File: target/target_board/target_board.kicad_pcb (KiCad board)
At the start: 2 copper layers, 76 x 68 mm, 72 parts, among them J1 USB_B_Micro, J2 SPI_CONN, J3 UART_CONN, J4 I2C_CONN, J5 SWD_CONN, J6 DFU, Q1 RZM001P02, Q2 RZM001P02, SW1 SW_Push, SW10 SW_Push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

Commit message: Continue layout
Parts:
- moved D3 7.20 mm to (34.7, 71.2)
- moved R8 6.62 mm to (34.6, 69.4), turned to 0 degrees
- moved D2 5.10 mm to (34.7, 67.6)
- moved R6 5.04 mm to (34.6, 65.8), turned to 0 degrees
- moved R5 4.00 mm to (34.6, 62.2), turned to 0 degrees
- moved D1 3.00 mm to (34.7, 64.0)
- moved R20 0.40 mm to (57.2, 73.5)
- moved R21 0.40 mm to (57.2, 72.0)
- moved R22 0.40 mm to (57.2, 70.5)
- moved R23 0.40 mm to (57.2, 69.0)
- moved R24 0.40 mm to (57.2, 67.5)
- moved R25 0.40 mm to (57.2, 66.0)
- moved R26 0.40 mm to (57.2, 64.5)
- moved R27 0.40 mm to (57.2, 63.0)
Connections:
- U3 pad 10: /LED_G -> /COL2
- U3 pad 11: /LED_Y -> /COL1
- U3 pad 12: /LED_R -> /ROW4
- U3 pad 13: Net-(U3-Pad13) -> /DISPA
- U3 pad 22: Net-(U3-Pad22) -> /DISPB
- U3 pad 39: /ROW4 -> /LED_R
- U3 pad 40: /DISPA -> Net-(U3-Pad40)
- U3 pad 41: /DISPB -> Net-(U3-Pad41)
- U3 pad 45: /COL1 -> /LED_Y
- U3 pad 46: /COL2 -> /LED_G
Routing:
- net VCC: track 0.00 -> 200.7 mm
- net /SCL: track 0.00 -> 111.2 mm, vias 0 -> 5
- net /SDA: track 0.00 -> 104.2 mm, vias 0 -> 5
- net /UART1_RX: track 0.00 -> 97.4 mm, vias 0 -> 2
- net /UART1_TX: track 0.00 -> 94.8 mm, vias 0 -> 2
- net GND: track 0.00 -> 50.3 mm, vias 0 -> 16
- net /ROW4: track 0.00 -> 36.0 mm
- net /ROW3: track 0.00 -> 36.0 mm
- net /ROW2: track 0.00 -> 36.0 mm
- net /ROW1: track 0.00 -> 36.0 mm
- net /COL3: track 0.00 -> 31.8 mm
- net /COL2: track 0.00 -> 31.8 mm
- net /COL1: track 0.00 -> 31.8 mm
- net /LED_G: track 0.00 -> 20.6 mm
- net /NRST: track 0.00 -> 19.5 mm
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- added copper zone on B.Cu, net GND

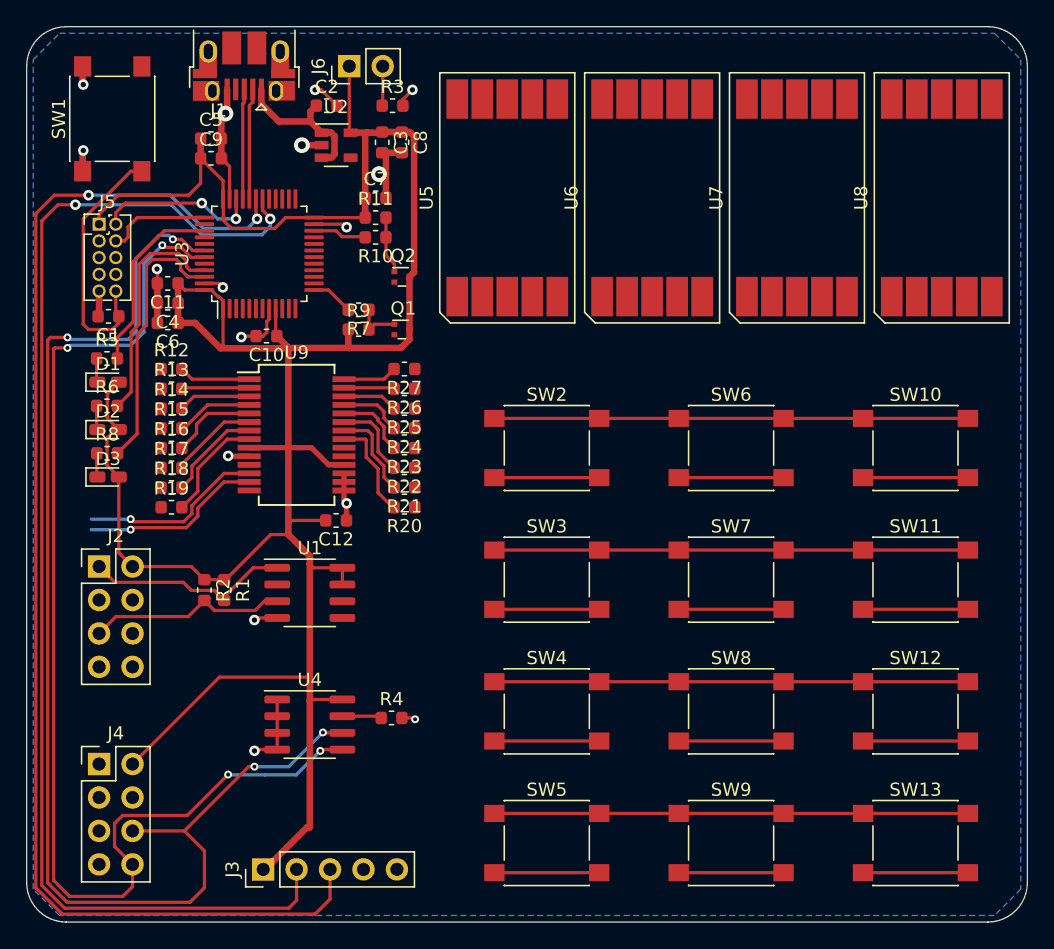
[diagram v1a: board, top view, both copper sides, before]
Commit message: Route busses.
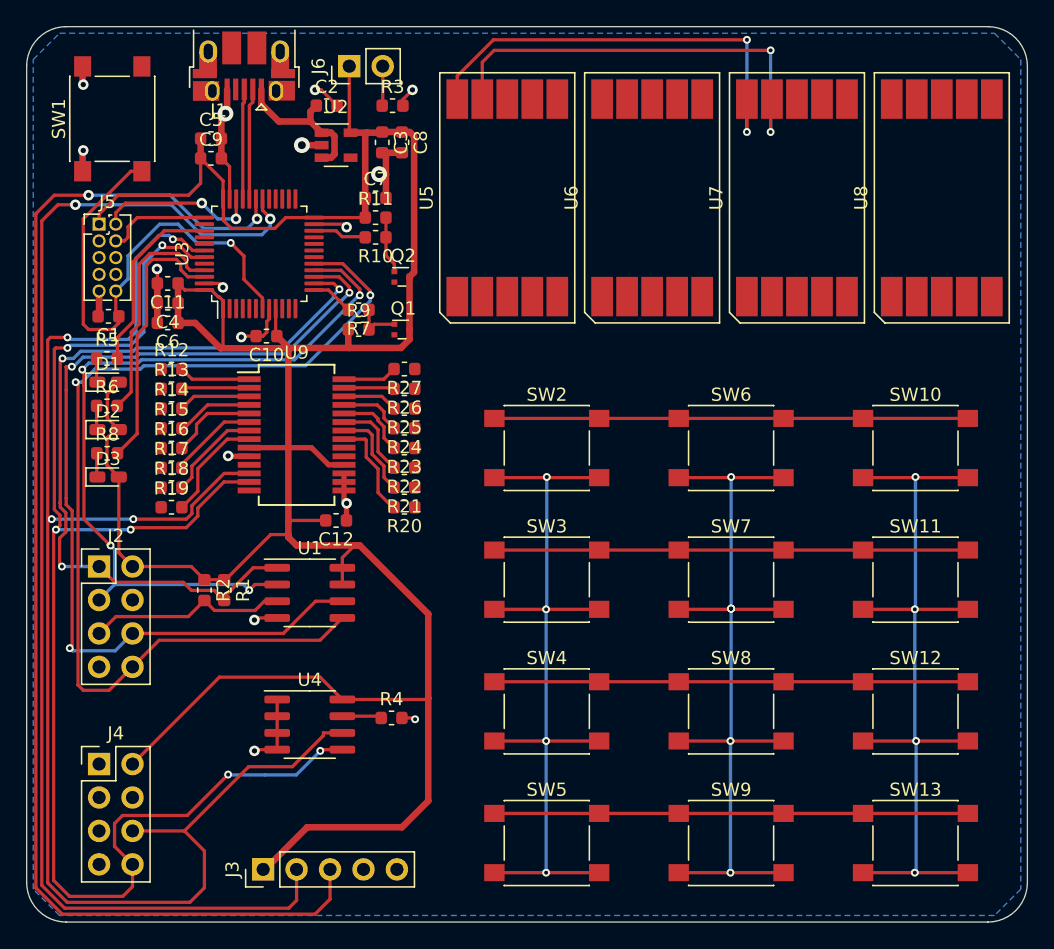
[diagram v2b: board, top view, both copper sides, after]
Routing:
- net /MOSI: track 0.00 -> 76.4 mm, vias 0 -> 2
- net /SCK: track 0.00 -> 71.2 mm, vias 0 -> 3
- net /MISO: track 0.00 -> 59.8 mm, vias 0 -> 4
- net /~CS: track 15.8 -> 60.4 mm, vias 0 -> 3
- net /A7: track 0.00 -> 34.4 mm, vias 0 -> 2
- net /A6: track 0.00 -> 33.8 mm, vias 0 -> 2
- net /COL3: track 31.8 -> 62.1 mm, vias 0 -> 4
- net /COL2: track 31.8 -> 62.0 mm, vias 0 -> 5
- net /COL1: track 31.8 -> 62.0 mm, vias 0 -> 4
- net VCC: track 200.7 -> 221.8 mm
- net /NRST: track 19.5 -> 38.0 mm, vias 0 -> 1
- net /SCL: track 111.2 -> 114.5 mm, vias 5 -> 4
- net /SDA: track 104.2 -> 107.2 mm, vias 5 -> 6

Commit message: Route most display
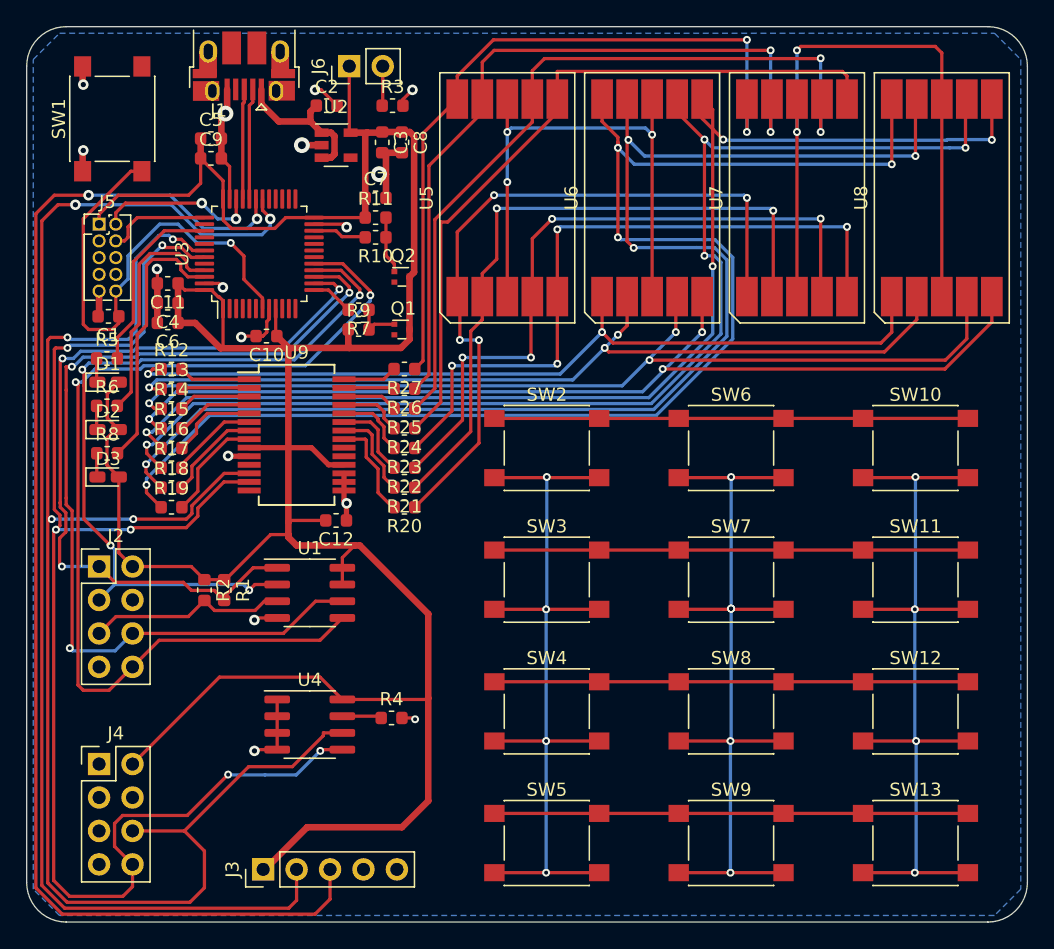
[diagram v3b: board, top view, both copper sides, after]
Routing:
- net /B7: track 0.00 -> 104.8 mm, vias 0 -> 4
- net /B6: track 0.00 -> 102.0 mm, vias 0 -> 4
- net /B4: track 0.00 -> 93.2 mm, vias 0 -> 4
- net /B5: track 0.00 -> 92.9 mm, vias 0 -> 4
- net /B3: track 0.00 -> 77.2 mm, vias 0 -> 3
- net /B2: track 0.00 -> 74.2 mm, vias 0 -> 3
- net /B1: track 0.00 -> 68.1 mm, vias 0 -> 3
- net /B0: track 0.00 -> 65.0 mm, vias 0 -> 2
- net /A5: track 0.00 -> 59.8 mm, vias 0 -> 2
- net /A4: track 0.00 -> 55.8 mm
- net /A0: track 0.00 -> 55.2 mm, vias 0 -> 4
- net /A3: track 0.00 -> 53.1 mm, vias 0 -> 4
- net /A2: track 0.00 -> 52.6 mm, vias 0 -> 4
- net /A1: track 0.00 -> 51.4 mm, vias 0 -> 2
- net Net-(Q2-Pad2): track 0.00 -> 51.0 mm, vias 0 -> 2
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
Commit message: Few airwires left.
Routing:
- net /ROW3: track 36.0 -> 127.1 mm, vias 0 -> 2
- net /ROW2: track 36.0 -> 115.1 mm, vias 0 -> 2
- net /ROW1: track 36.0 -> 102.3 mm, vias 0 -> 2
- net Net-(Q2-Pad2): track 51.0 -> 89.3 mm, vias 2 -> 4
- net Net-(Q1-Pad2): track 41.3 -> 55.6 mm, vias 3 -> 5
- net /A1: track 51.4 -> 52.3 mm
- net /B7: track 104.8 -> 105.6 mm

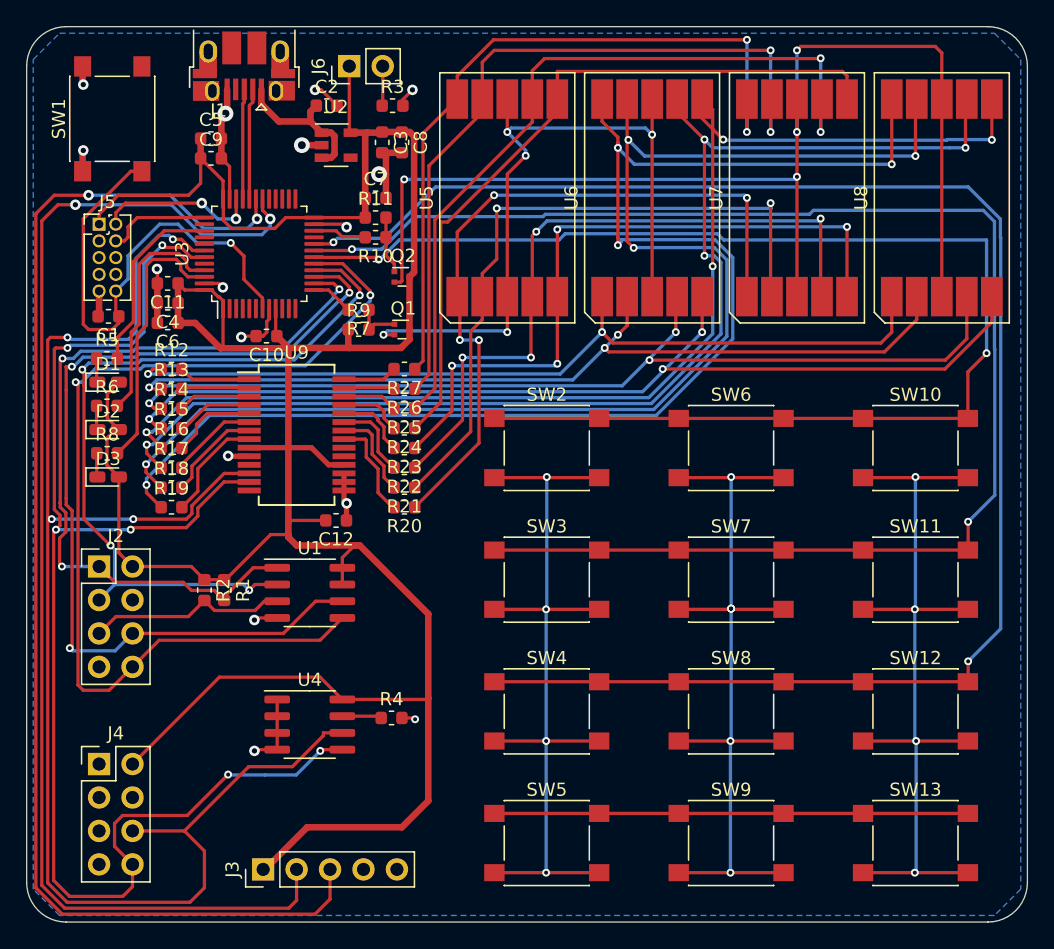
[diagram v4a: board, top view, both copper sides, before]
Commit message: Finish routing.
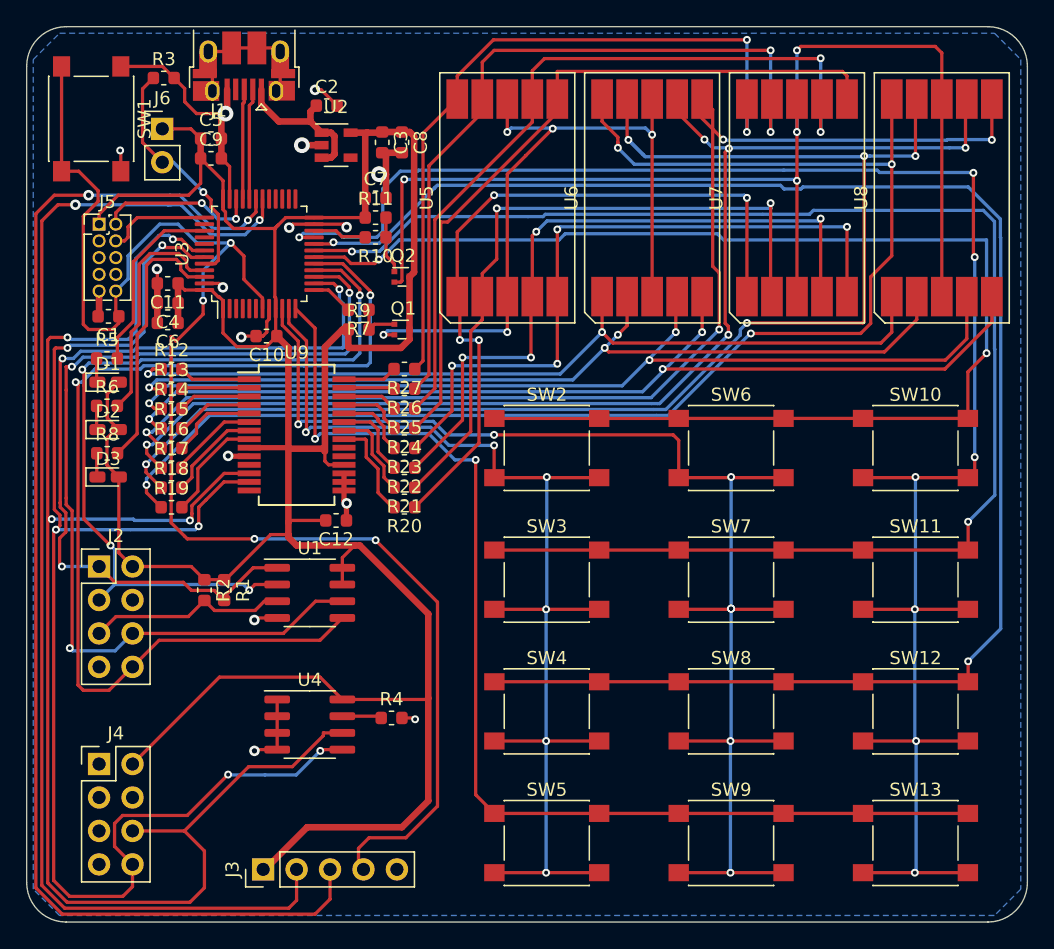
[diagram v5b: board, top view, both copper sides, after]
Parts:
- moved R3 17.5 mm to (38.9, 40.9)
- moved J6 15.0 mm to (38.8, 44.8), turned to 0 degrees
- moved SW1 1.60 mm to (33.4, 44.0), turned to 270 degrees
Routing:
- net /COL3: track 62.1 -> 142.3 mm, vias 4 -> 8
- net /NRST: track 38.0 -> 117.1 mm, vias 1 -> 4
- net /ROW4: track 36.0 -> 87.1 mm, vias 0 -> 2
- net /COL2: track 62.0 -> 103.7 mm, vias 5 -> 7
- net /COL1: track 62.0 -> 89.4 mm, vias 4 -> 6
- net /BOOT0: track 3.02 -> 18.2 mm, vias 0 -> 1
- net Net-(J1-Pad6): track 0.00 -> 11.8 mm
- net GND: track 50.3 -> 59.4 mm, vias 16 -> 15
- net VCC: track 221.8 -> 226.8 mm
- net /B6: track 102.0 -> 105.8 mm, vias 4 -> 5
- net /~CS: track 60.4 -> 63.6 mm
- net /MOSI: track 76.4 -> 79.3 mm
- net /SCK: track 71.2 -> 73.9 mm
- net /MISO: track 59.8 -> 62.3 mm
- net /UART1_TX: track 94.8 -> 93.8 mm
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
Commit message: Make board smaller.
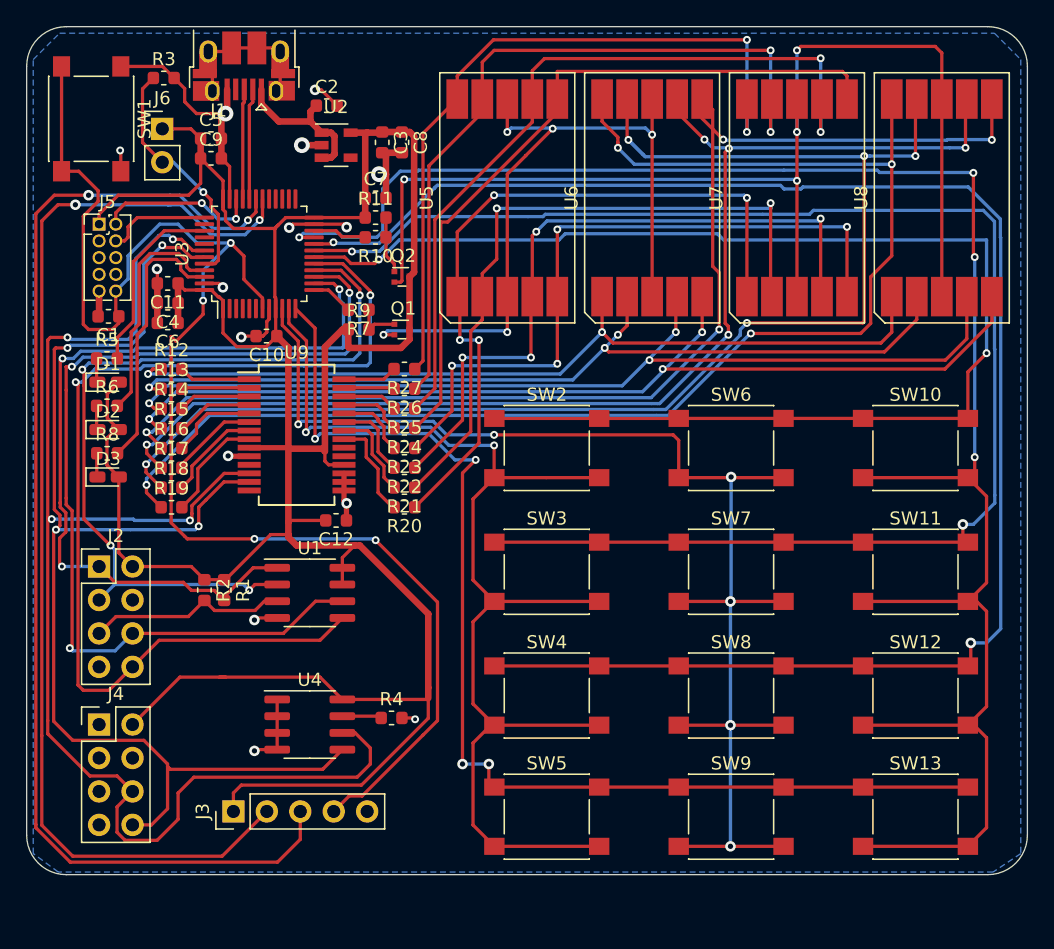
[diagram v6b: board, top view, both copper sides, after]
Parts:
- moved J3 4.95 mm to (44.2, 96.6)
- moved J4 3.00 mm to (34.0, 90.0)
- moved SW13 2.00 mm to (96.0, 97.0)
- moved SW5 2.00 mm to (68.0, 97.0)
- moved SW9 2.00 mm to (82.0, 97.0)
- moved SW12 1.20 mm to (96.0, 87.8)
- moved SW4 1.20 mm to (68.0, 87.8)
- moved SW8 1.20 mm to (82.0, 87.8)
- moved SW11 0.60 mm to (96.0, 78.4)
- moved SW3 0.60 mm to (68.0, 78.4)
- moved SW7 0.60 mm to (82.0, 78.4)
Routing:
- net /SDA: track 107.7 -> 94.3 mm, vias 6 -> 4
- net /SCL: track 114.8 -> 105.1 mm
- net /UART1_TX: track 93.8 -> 86.0 mm
- net /UART1_RX: track 97.0 -> 90.5 mm
- net /NRST: track 117.1 -> 112.3 mm
- net VCC: track 226.8 -> 224.4 mm
- net /COL1: track 89.4 -> 91.5 mm, vias 6 -> 2
- net /COL3: track 142.3 -> 144.3 mm, vias 8 -> 4
- net /COL2: track 103.7 -> 101.8 mm, vias 7 -> 6
- net /ROW4: vias 2 -> 4
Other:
- board size 76 x 68 mm -> 76 x 64.4 mm

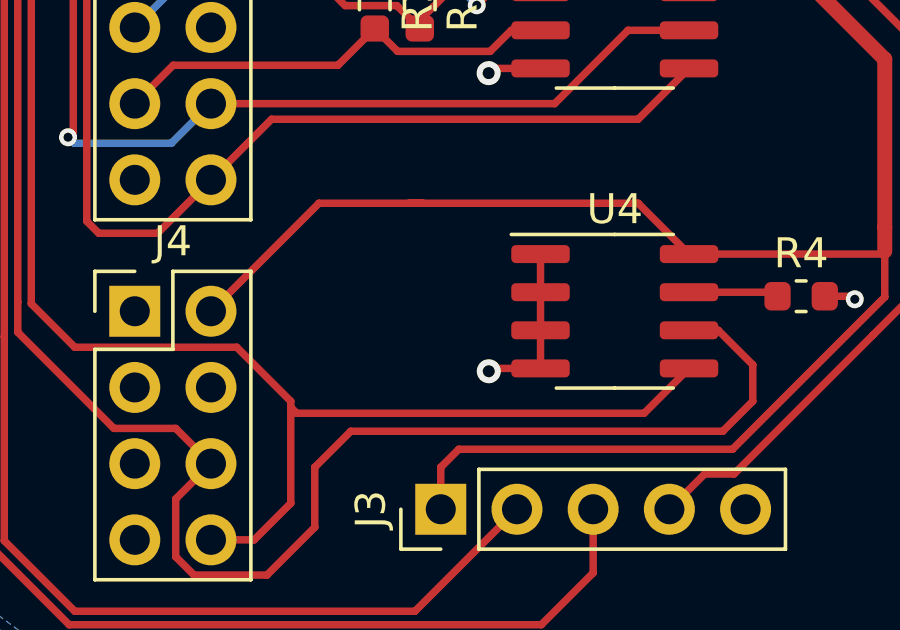
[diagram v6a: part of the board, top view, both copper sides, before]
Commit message: Add missing I2C pullups
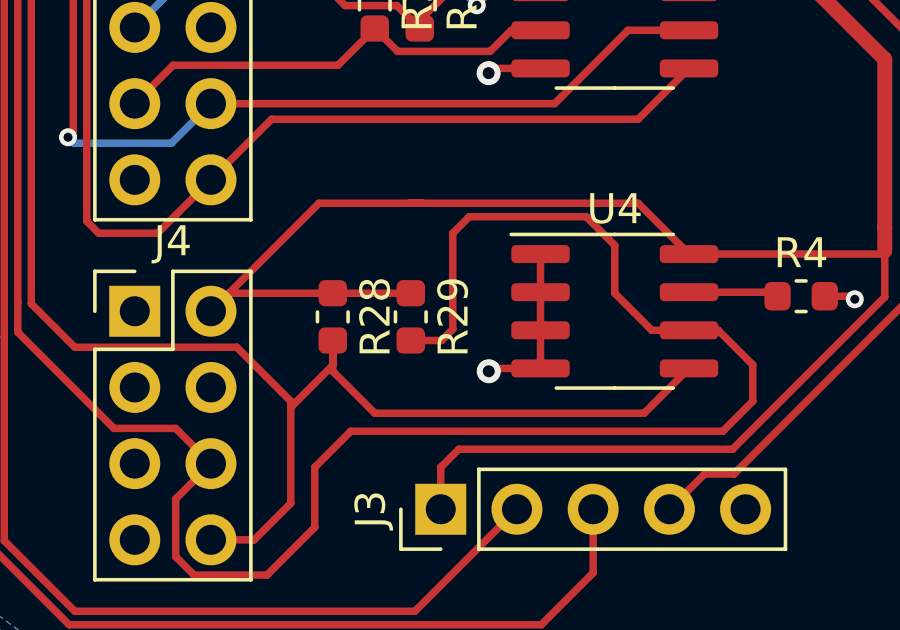
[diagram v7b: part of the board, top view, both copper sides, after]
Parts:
- added R28: 2.2k, Resistor_SMD:R_0603_1608Metric, F.Cu at (40.6, 90.2)
- added R29: 2.2k, Resistor_SMD:R_0603_1608Metric, F.Cu at (43.2, 90.2)
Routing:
- net /SCL: track 105.1 -> 120.5 mm
- net VCC: track 224.4 -> 231.4 mm
- net /SDA: track 94.3 -> 97.2 mm
